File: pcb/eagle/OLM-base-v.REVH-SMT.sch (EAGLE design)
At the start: 55 parts, among them CN1 MiniB USB, IC1 LP2985-3.3v, IC2 ATMEGA32U4-AU, IC3 DS1307, IC4 ENC28J60, T1 IRLML2246, U1 USD-SOCKETMICRO-SD-SOCKET-TAO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, X1 8MHz, X2 32.657k, X2A 25MHz, X2A1 25MHz

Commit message: rewired surface mount version
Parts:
- removed CAP: 10u, resistor:C-EUC0805
- removed R7, R8: 330, rcl:R-EU_R0805
- removed RBS: 2.32K, rcl:R-EU_R0805
- removed RCL, RDA: 10K, rcl:R-EU_R0805
- removed X2A1: 25MHz, SparkFun:CRYSTALHC49US
- added CAP1: 10u, resistor:C-EUC0805
- added RBS1: 2.32K, rcl:R-EU_R0805
- added REA, REB: 330, rcl:R-EU_R0805
- added RN2: (no value), resistor-dil:4R-NEXB38V
- C11: value 0.1µ -> 0.1u; device resistor:C-EUC0805 -> rcl:C-EUC0805
- C9: value 0.1u -> 0.1µ; device rcl:C-EUC0805 -> resistor:C-EUC0805
- IC3: value DS1307 -> ENC28J60; device adafruit:DS1307SOIC -> SparkFun:ENC28J60SO28LONG
- IC4: value ENC28J60 -> DS1307; device SparkFun:ENC28J60SO28LONG -> adafruit:DS1307SOIC
- X2: value 32.657k -> 32.768kHz
- renumbered RXLED to RX, TXLED to TX
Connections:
- removed net MISO/D12: CON1.5, CON2.5, CON3.5
- removed net MOSI/D11: CON1.3, CON2.3, CON3.3
- removed net N$34: IC4.LEDA, R7.1
- removed net N$36: BAT1.+, IC3.VBAT
- removed net N$37: IC4.LEDB, R8.1
- removed net N$39: CAP.1, IC4.VCAP
- removed net N$41: CX1.1, IC4.OSC2, X2A.2, X2A1.2
- removed net N$42: CX2.1, IC4.OSC1, X2A.1, X2A1.1
- removed net N$47: IC3.X1, X2.1
- removed net N$50: IC3.X2, X2.2
- removed net N$54: C10.2, RN1C.2, RN1D.2
- removed net N$59: IC4.RBIAS, RBS.2
- removed net SCK/D13: CON1.1, CON2.1, CON3.1
- new net N$10: C9.2, RN1C.2, RN1D.2
- new net N$14: IC3.LEDA, REA.1
- new net N$15: IC3.LEDB, REB.1
- new net N$16: CAP1.1, IC3.VCAP
- new net N$17: IC3.RBIAS, RBS1.2
- new net N$18: CX1.1, IC3.OSC2, X2A.2
- new net N$19: CX2.1, IC3.OSC1, X2A.1
- new net N$20: BAT1.+, IC4.VBAT
- new net N$21: IC4.X1, X2.2
- new net N$30: IC4.X2, X2.1
- net +3V3: now also C11.1, IC3.VDD, IC3.VDDOSC, IC3.VDDPLL, IC3.VDDRX, IC3.VDDTX, IC4.VCC, JP3.8, RN2A.2, RN2B.2; no longer C9.1, IC3.VCC, IC4.VDD, IC4.VDDOSC, IC4.VDDPLL, IC4.VDDRX, IC4.VDDTX, RCL.1, RDA.1
- net D2/SDA: now also IC4.SDA, RN2B.1; no longer IC3.SDA, RDA.2
- net D3/SCL: now also IC4.SCL, RN2A.1; no longer IC3.SCL, RCL.2
- net D4/A6: now also IC3.RESET; no longer IC4.RESET
- net D6*/A8: now also IC3.CS; no longer IC4.CS
- net E-CLK: now also IC3.CLKOUT; no longer IC4.CLKOUT
- net E-INT: now also IC3./INT; no longer IC4./INT
- net GND: now also C11.2, C9.1, CAP1.2, IC3.VSS, IC3.VSSOSC, IC3.VSSPLL, IC3.VSSRX, IC3.VSSTX, IC4.GND, RBS1.1, U1.SHIELD@1, U1.SHIELD@2, U1.SHIELD@3, U1.SHIELD@4; no longer C11.1, C9.2, CAP.2, IC3.GND, IC4.VSS, IC4.VSSOSC, IC4.VSSPLL, IC4.VSSRX, IC4.VSSTX, RBS.1
- net LEDA: now also REA.2; no longer R7.2
- net LEDB: now also REB.2; no longer R8.2
- net MISO: now also CON1.5, CON2.5, CON3.5, IC3.SO; no longer IC4.SO
- net MOSI: now also CON1.3, CON2.3, CON3.3, IC3.SI; no longer IC4.SI
- net RD+: now also IC3.TPIN+; no longer IC4.TPIN+
- net RD-: now also IC3.TPIN-; no longer IC4.TPIN-
- net SCK: now also CON1.1, CON2.1, CON3.1, IC3.SCK; no longer IC4.SCK
- net TCT: now also C10.2; no longer C11.2
- net TD+: now also IC3.TPOUT+; no longer IC4.TPOUT+
- net TD-: now also IC3.TPOUT-; no longer IC4.TPOUT-
- net VCC: no longer JP3.8
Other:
- moved on the sheet: BAT1, C10, C11, C9, CX1, CX2, L2, RN1A, RN1B, RN1C, RN1D, U1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

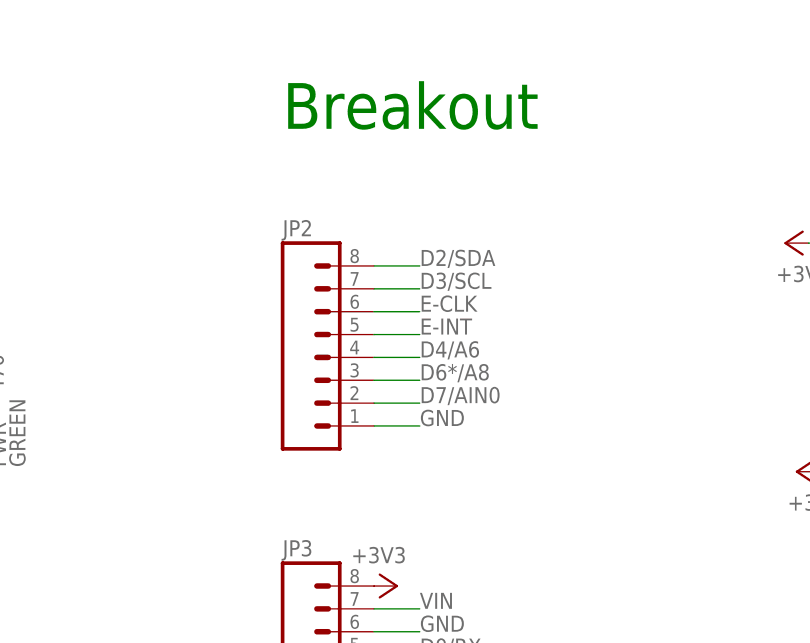
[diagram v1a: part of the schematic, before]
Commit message: fixed breakouts by adding reset pin
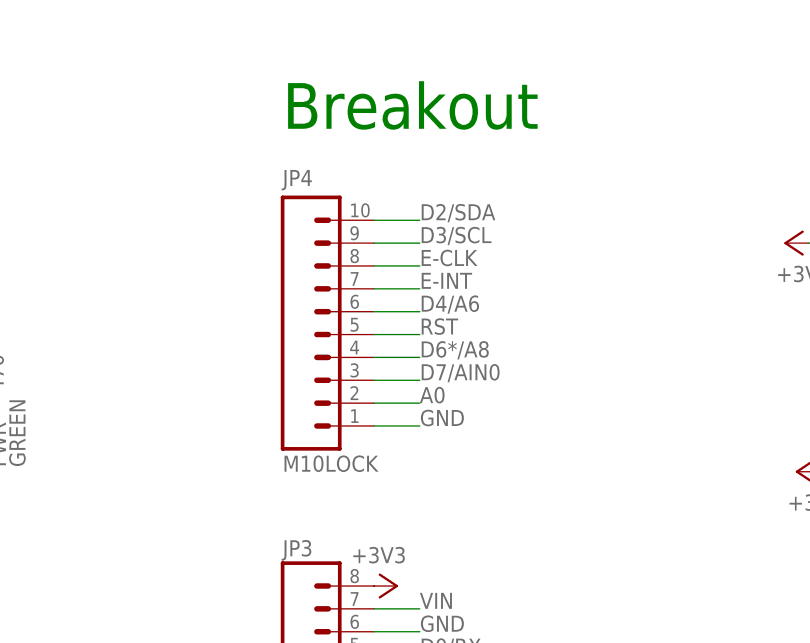
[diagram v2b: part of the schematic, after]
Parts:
- removed JP2: (no value), SparkFun-Connectors:M08LOCK
- added JP4: M10LOCK, SparkFun-Connectors:M10LOCK
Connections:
- net A0: now also JP4.2
- net D2/SDA: now also JP4.10; no longer JP2.8
- net D3/SCL: now also JP4.9; no longer JP2.7
- net D4/A6: now also JP4.6; no longer JP2.4
- net D6*/A8: now also JP4.4; no longer JP2.3
- net D7/AIN0: now also JP4.3; no longer JP2.2
- net E-CLK: now also JP4.8; no longer JP2.6
- net E-INT: now also JP4.7; no longer JP2.5
- net GND: now also JP4.1; no longer JP2.1
- net RST: now also JP4.5
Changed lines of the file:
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@@
 <setting verticaltext="up"/>
 </settings>
-<grid distance="0.05" unitdist="inch" unit="inch" style="lines" multiple="1" display="no" altdistance="0.01" altunitdist="inch" altunit="inch"/>
+<grid distance="0.1" unitdist="inch" unit="inch" style="lines" multiple="1" display="no" altdistance="0.01" altunitdist="inch" altunit="inch"/>
 <layers>
 <layer number="1" name="Top" color="4" fill="1" visible="no" active="no"/>
@@
 <part name="+3V12" library="supply1" deviceset="+3V3" device=""/>
 <part name="JP3" library="SparkFun-Connectors" deviceset="M08" device="LOCK"/>
-<part name="JP2" library="SparkFun-Connectors" deviceset="M08" device="LOCK"/>
 <part name="U1" library="SparkFunNew" deviceset="USD-SOCKET" device="MICRO-SD-SOCKET-TAOBAO" value="USD-SOCKETMICRO-SD-SOCKET-TAOBAO"/>
 <part name="GND10" library="SparkFun" deviceset="GND" device=""/>
@@
 <part name="X2A" library="SparkFun" deviceset="CRYSTAL" device="10.5X4.8" value="25MHz"/>
 <part name="+3V2" library="supply1" deviceset="+3V3" device=""/>
+<part name="JP4" library="SparkFun-Connectors" deviceset="M10" device="LOCK"/>
 </parts>
 <sheets>
@@
 <instance part="+3V12" gate="G$1" x="101.6" y="142.24" rot="R90"/>
 <instance part="JP3" gate="G$1" x="50.8" y="147.32"/>
-<instance part="JP2" gate="G$1" x="50.8" y="182.88"/>
 <instance part="U1" gate="G$1" x="-6.35" y="29.21"/>
 <instance part="GND10" gate="1" x="-13.97" y="8.89"/>
@@
 <instance part="X2A" gate="G$1" x="242.57" y="182.88" smashed="yes" rot="R90"/>
 <instance part="+3V2" gate="G$1" x="58.42" y="157.48" rot="R270"/>
+<instance part="JP4" gate="G$1" x="45.72" y="193.04"/>
 </instances>
 <busses>
@@
 <wire x1="55.88" y1="152.4" x2="60.96" y2="152.4" width="0.1524" layer="91"/>
 <label x="60.96" y="152.4" size="1.778" layer="95"/>
-</segment>
-<segment>
-<pinref part="JP2" gate="G$1" pin="1"/>
-<wire x1="55.88" y1="175.26" x2="60.96" y2="175.26" width="0.1524" layer="91"/>
-<label x="60.96" y="175.26" size="1.778" layer="95"/>
 </segment>
 <segment>
@@
 <pinref part="GND24" gate="1" pin="GND"/>
 </segment>
+<segment>
+<wire x1="55.88" y1="175.26" x2="60.96" y2="175.26" width="0.1524" layer="91"/>
+<label x="60.96" y="175.26" size="1.778" layer="95"/>
+<pinref part="JP4" gate="G$1" pin="1"/>
+</segment>
 </net>
 <net name="+5V" class="0">
@@
 <pinref part="BOOT" gate="G$1" pin="P"/>
 <junction x="124.46" y="88.9"/>
+</segment>
+<segment>
+<wire x1="55.88" y1="185.42" x2="60.96" y2="185.42" width="0.1524" layer="91"/>
+<label x="60.96" y="185.42" size="1.778" layer="95"/>
+<pinref part="JP4" gate="G$1" pin="5"/>
 </segment>
 </net>
@@
 </segment>
 <segment>
-<pinref part="JP2" gate="G$1" pin="2"/>
-<wire x1="55.88" y1="177.8" x2="60.96" y2="177.8" width="0.1524" layer="91"/>
-<label x="60.96" y="177.8" size="1.778" layer="95"/>
-</segment>
-<segment>
 <pinref part="U1" gate="G$1" pin="CS"/>
 <wire x1="-13.97" y1="39.37" x2="-22.86" y2="39.37" width="0.1524" layer="91"/>
 <label x="-21.59" y="39.37" size="1.778" layer="95"/>
+</segment>
+<segment>
+<wire x1="55.88" y1="180.34" x2="60.96" y2="180.34" width="0.1524" layer="91"/>
+<label x="60.96" y="180.34" size="1.778" layer="95"/>
+<pinref part="JP4" gate="G$1" pin="3"/>
 </segment>
 </net>
@@
 </segment>
 <segment>
-<pinref part="JP2" gate="G$1" pin="3"/>
-<wire x1="55.88" y1="180.34" x2="60.96" y2="180.34" width="0.1524" layer="91"/>
-<label x="60.96" y="180.34" size="1.778" layer="95"/>
-</segment>
-<segment>
 <wire x1="251.46" y1="191.77" x2="238.76" y2="191.77" width="0.1524" layer="91"/>
 <label x="241.3" y="191.77" size="1.778" layer="95"/>
 <pinref part="IC3" gate="G$1" pin="CS"/>
+</segment>
+<segment>
+<wire x1="55.88" y1="182.88" x2="60.96" y2="182.88" width="0.1524" layer="91"/>
+<label x="60.96" y="182.88" size="1.778" layer="95"/>
+<pinref part="JP4" gate="G$1" pin="4"/>
 </segment>
 </net>
@@
 <label x="118.11" y="193.04" size="1.778" layer="95"/>
 </segment>
+<segment>
+<wire x1="55.88" y1="177.8" x2="60.96" y2="177.8" width="0.1524" layer="91"/>
+<label x="60.96" y="177.8" size="1.778" layer="95"/>
+<pinref part="JP4" gate="G$1" pin="2"/>
+</segment>
 </net>
 <net name="IO11*" class="0">
@@
 <label x="182.88" y="17.78" size="1.778" layer="95"/>
 <pinref part="IC2" gate="G$1" pin="PD1(INT1/SDA)"/>
-</segment>
-<segment>
-<pinref part="JP2" gate="G$1" pin="8"/>
-<wire x1="55.88" y1="193.04" x2="60.96" y2="193.04" width="0.1524" layer="91"/>
-<label x="60.96" y="193.04" size="1.778" layer="95"/>
 </segment>
 <segment>
@@
 <junction x="393.7" y="34.29"/>
 </segment>
+<segment>
+<wire x1="55.88" y1="198.12" x2="60.96" y2="198.12" width="0.1524" layer="91"/>
+<label x="60.96" y="198.12" size="1.778" layer="95"/>
+<pinref part="JP4" gate="G$1" pin="10"/>
+</segment>
 </net>
 <net name="D3/SCL" class="0">
@@
 <label x="182.88" y="15.24" size="1.778" layer="95"/>
 <pinref part="IC2" gate="G$1" pin="PD0(INT0/OC0B)"/>
-</segment>
-<segment>
-<pinref part="JP2" gate="G$1" pin="7"/>
-<wire x1="55.88" y1="190.5" x2="60.96" y2="190.5" width="0.1524" layer="91"/>
-<label x="60.96" y="190.5" size="1.778" layer="95"/>
 </segment>
 <segment>
@@
 <junction x="397.51" y="39.37"/>
 </segment>
+<segment>
+<wire x1="55.88" y1="195.58" x2="60.96" y2="195.58" width="0.1524" layer="91"/>
+<label x="60.96" y="195.58" size="1.778" layer="95"/>
+<pinref part="JP4" gate="G$1" pin="9"/>
+</segment>
 </net>
 <net name="D4/A6" class="0">
@@
 </segment>
 <segment>
-<pinref part="JP2" gate="G$1" pin="4"/>
-<wire x1="55.88" y1="182.88" x2="60.96" y2="182.88" width="0.1524" layer="91"/>
-<label x="60.96" y="182.88" size="1.778" layer="95"/>
-</segment>
-<segment>
 <wire x1="251.46" y1="194.31" x2="238.76" y2="194.31" width="0.1524" layer="91"/>
 <label x="241.3" y="194.31" size="1.778" layer="95"/>
 <pinref part="IC3" gate="G$1" pin="RESET"/>
 </segment>
-</net>
-<net name="E-CLK" class="0">
-<segment>
-<pinref part="JP2" gate="G$1" pin="6"/>
+<segment>
 <wire x1="55.88" y1="187.96" x2="60.96" y2="187.96" width="0.1524" layer="91"/>
 <label x="60.96" y="187.96" size="1.778" layer="95"/>
-</segment>
+<pinref part="JP4" gate="G$1" pin="6"/>
+</segment>
+</net>
+<net name="E-CLK" class="0">
 <segment>
 <wire x1="287.02" y1="158.75" x2="293.37" y2="158.75" width="0.1524" layer="91"/>
@@
 <pinref part="IC3" gate="G$1" pin="CLKOUT"/>
 </segment>
+<segment>
+<wire x1="55.88" y1="193.04" x2="60.96" y2="193.04" width="0.1524" layer="91"/>
+<label x="60.96" y="193.04" size="1.778" layer="95"/>
+<pinref part="JP4" gate="G$1" pin="8"/>
+</segment>
 </net>
 <net name="E-INT" class="0">
-<segment>
-<pinref part="JP2" gate="G$1" pin="5"/>
-<wire x1="55.88" y1="185.42" x2="60.96" y2="185.42" width="0.1524" layer="91"/>
-<label x="60.96" y="185.42" size="1.778" layer="95"/>
-</segment>
 <segment>
 <wire x1="285.75" y1="161.29" x2="287.02" y2="161.29" width="0.1524" layer="91"/>
@@
 <junction x="287.02" y="161.29"/>
 </segment>
-</net>
+<segment>
+<wire x1="55.88" y1="190.5" x2="60.96" y2="190.5" width="0.1524" layer="91"/>
+<label x="60.96" y="190.5" size="1.778" layer="95"/>
+<pinref part="JP4" gate="G$1" pin="7"/>
+</segment>
+</net>
